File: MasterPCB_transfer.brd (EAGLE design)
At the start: 160.4 x 165.1 mm, 1072 parts, among them IC1 NCS21911SN2T1G, IC10 LDL1117S33R, IC11 LTC4222CUH#PBF, IC12 LTC4222CUH#PBF, IC13 LTC4222CUH#PBF, IC14 LTC4222CUH#PBF, IC15 LTC4222CUH#PBF, IC16 LTC4222CUH#PBF, IC17 LTC4222CUH#PBF, IC18 LTC4222CUH#PBF, IC19 LTC4222CUH#PBF, IC2 NCS21911SN2T1G, IC20 LTC4222CUH#PBF, IC21 LTC4222CUH#PBF, IC22 LTC4222CUH#PBF, IC23 LTC4222CUH#PBF, IC24 NCS21911SN2T1G, IC25 NCS21911SN2T1G, IC26 NCS21911SN2T1G, IC27 NCS21911SN2T1G, IC28 NCS21911SN2T1G, IC29 NCS21911SN2T1G, IC3 NCS21911SN2T1G, IC30 NCS21911SN2T1G, IC31 ADIS16500AMLZ, IC32 LTC6820IUD#PBF, IC33 CBTL01023GM,115, IC34 MAX889TESA+, IC35 NCS21911SN2T1G, IC36 NCS21911SN2T1G, IC37 NCS21911SN2T1G, IC38 ADS8588HIPM, IC39 NCS21911SN2T1G, IC4 LTC4222CUH#PBF, IC40 NCS21911SN2T1G, IC41 NCS21911SN2T1G, IC42 NCS21911SN2T1G, IC43 NCS21911SN2T1G, IC44 NCS21911SN2T1G, IC45 NCS21911SN2T1G, IC46 NCS21911SN2T1G, IC47 NCS21911SN2T1G, IC48 NCS21911SN2T1G, IC49 NCS21911SN2T1G, IC5 LP38692SDX-5.0_NOPB, IC50 NCS21911SN2T1G, IC51 ADS8588HIPM, IC52 ADS8588HIPM, IC53 NCS21911SN2T1G, IC54 NCS21911SN2T1G, IC55 NCS21911SN2T1G, IC56 NCS21911SN2T1G, IC57 NCS21911SN2T1G, IC58 NCS21911SN2T1G, IC59 NCS21911SN2T1G, IC6 LP38692SDX-5.0_NOPB, IC60 NCS21911SN2T1G, IC61 NCS21911SN2T1G, IC62 NCS21911SN2T1G, IC63 NCS21911SN2T1G, IC64 NCS21911SN2T1G, IC65 NCS21911SN2T1G, IC66 NCS21911SN2T1G, IC67 NCS21911SN2T1G, IC68 NCS21911SN2T1G, IC69 NCS21911SN2T1G, IC7 LDL1117S33R, IC70 NCS21911SN2T1G, IC71 NCS21911SN2T1G, IC72 NCS21911SN2T1G, IC73 NCS21911SN2T1G, IC74 NCS21911SN2T1G, IC75 NCS21911SN2T1G, IC76 NCS21911SN2T1G, IC77 NCS21911SN2T1G, IC78 NCS21911SN2T1G, IC79 NCS21911SN2T1G, IC8 LDL1117S33R, IC9 LP38692SDX-5.0_NOPB, J1 SAMTEC-SMM-104-02-X-DJ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

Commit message: Save point
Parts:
- moved C196 2.19 mm to (89.4, 42.2)
- moved C14 2.19 mm to (92.5, 26.8)
- moved C17 2.19 mm to (76.3, 31.9)
- moved C19 2.19 mm to (77.1, 29.9)
- moved C20 2.19 mm to (77.1, 36.3)
- moved C21 2.19 mm to (77.1, 38.4)
- moved C23 2.19 mm to (86.1, 42.2)
- moved C24 2.19 mm to (83.5, 42.3)
- moved C25 2.19 mm to (76.3, 34.3)
- moved IC52 2.19 mm to (86.3, 33.1)
- moved R503 1.51 mm to (130.0, 65.7)
- moved R504 1.31 mm to (132.3, 61.1)
- moved R471 0.94 mm to (130.0, 61.1)
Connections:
- removed net PG7: J12.23
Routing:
- net PF1: track 0.00 -> 77.4 mm, vias 0 -> 2
- net PG0: track 0.00 -> 77.3 mm, vias 0 -> 2
- net PG1: track 0.00 -> 71.4 mm, vias 0 -> 2
- net PG9: track 0.00 -> 71.2 mm, vias 0 -> 2
- net PG12: track 0.00 -> 71.1 mm, vias 0 -> 2
- net PG10: track 0.00 -> 68.6 mm, vias 0 -> 2
- net PG15: track 0.00 -> 62.8 mm, vias 0 -> 2
- net PG6: track 0.00 -> 57.7 mm, vias 0 -> 2
- net PG8: track 0.00 -> 56.8 mm, vias 0 -> 2
- net PG5: track 0.00 -> 54.4 mm, vias 0 -> 2
- net PG4: track 0.00 -> 52.8 mm, vias 0 -> 2
- net PG14: track 0.00 -> 52.3 mm, vias 0 -> 2
- net GND: track 0.00 -> 50.5 mm, vias 0 -> 30
- net PG3: track 0.00 -> 50.0 mm, vias 0 -> 2
- net PG2: track 0.00 -> 48.8 mm, vias 0 -> 2
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
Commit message: save point
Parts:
- moved J4 4.44 mm to (79.8, 81.9)
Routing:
- net PF11: track 0.00 -> 75.0 mm, vias 0 -> 2
- net PE6: track 0.00 -> 71.5 mm, vias 0 -> 2
- net PF2: track 0.00 -> 70.8 mm, vias 0 -> 2
- net PF9: track 0.00 -> 68.5 mm, vias 0 -> 2
- net PF8: track 0.00 -> 67.3 mm, vias 0 -> 2
- net PF3: track 0.00 -> 60.7 mm, vias 0 -> 2
- net PF6: track 0.00 -> 58.2 mm, vias 0 -> 2
- net PF7: track 0.00 -> 55.1 mm, vias 0 -> 2
- net PE5: track 0.00 -> 52.2 mm, vias 0 -> 2
- net PF10: track 0.00 -> 48.6 mm, vias 0 -> 2
- net PF4: track 0.00 -> 36.8 mm, vias 0 -> 2
- net PF5: track 0.00 -> 32.6 mm, vias 0 -> 2

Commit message: Save point
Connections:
- removed net PB13: J14.67
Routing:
- net PE0: track 0.00 -> 86.6 mm, vias 0 -> 2
- net PD15: track 0.00 -> 69.8 mm, vias 0 -> 2
- net PE1: track 0.00 -> 69.2 mm, vias 0 -> 2
- net PD14: track 0.00 -> 68.3 mm, vias 0 -> 2
- net PA3: track 0.00 -> 67.0 mm, vias 0 -> 2
- net PA12: track 0.00 -> 65.7 mm, vias 0 -> 2
- net PA5: track 0.00 -> 65.5 mm, vias 0 -> 2
- net PD11: track 0.00 -> 65.0 mm, vias 0 -> 2
- net PB7: track 0.00 -> 63.3 mm, vias 0 -> 2
- net PA6: track 0.00 -> 62.5 mm, vias 0 -> 2
- net PD12: track 0.00 -> 62.0 mm, vias 0 -> 2
- net PD13: track 0.00 -> 60.1 mm, vias 0 -> 2
- net PA11: track 0.00 -> 59.6 mm, vias 0 -> 2
- net PA10: track 0.00 -> 55.5 mm, vias 0 -> 2
- net PE3: track 0.00 -> 50.7 mm, vias 0 -> 2
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
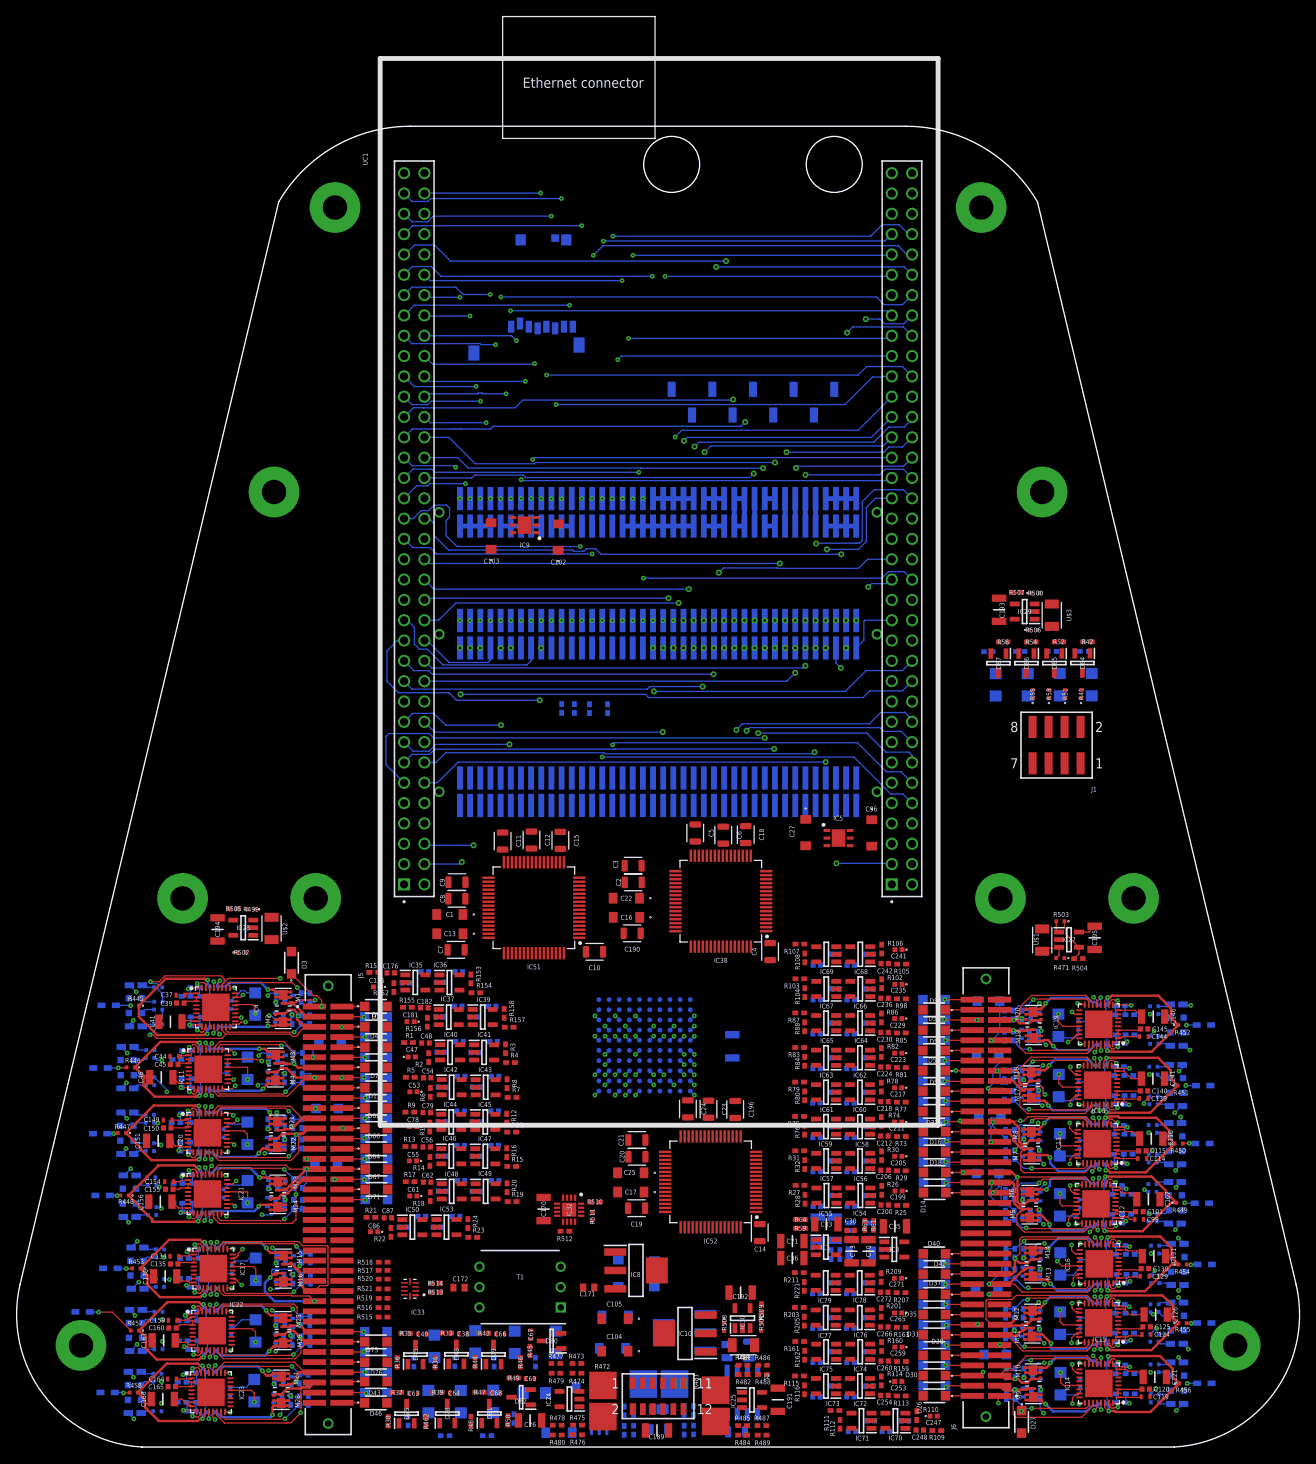
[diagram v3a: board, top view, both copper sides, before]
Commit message: New board shape
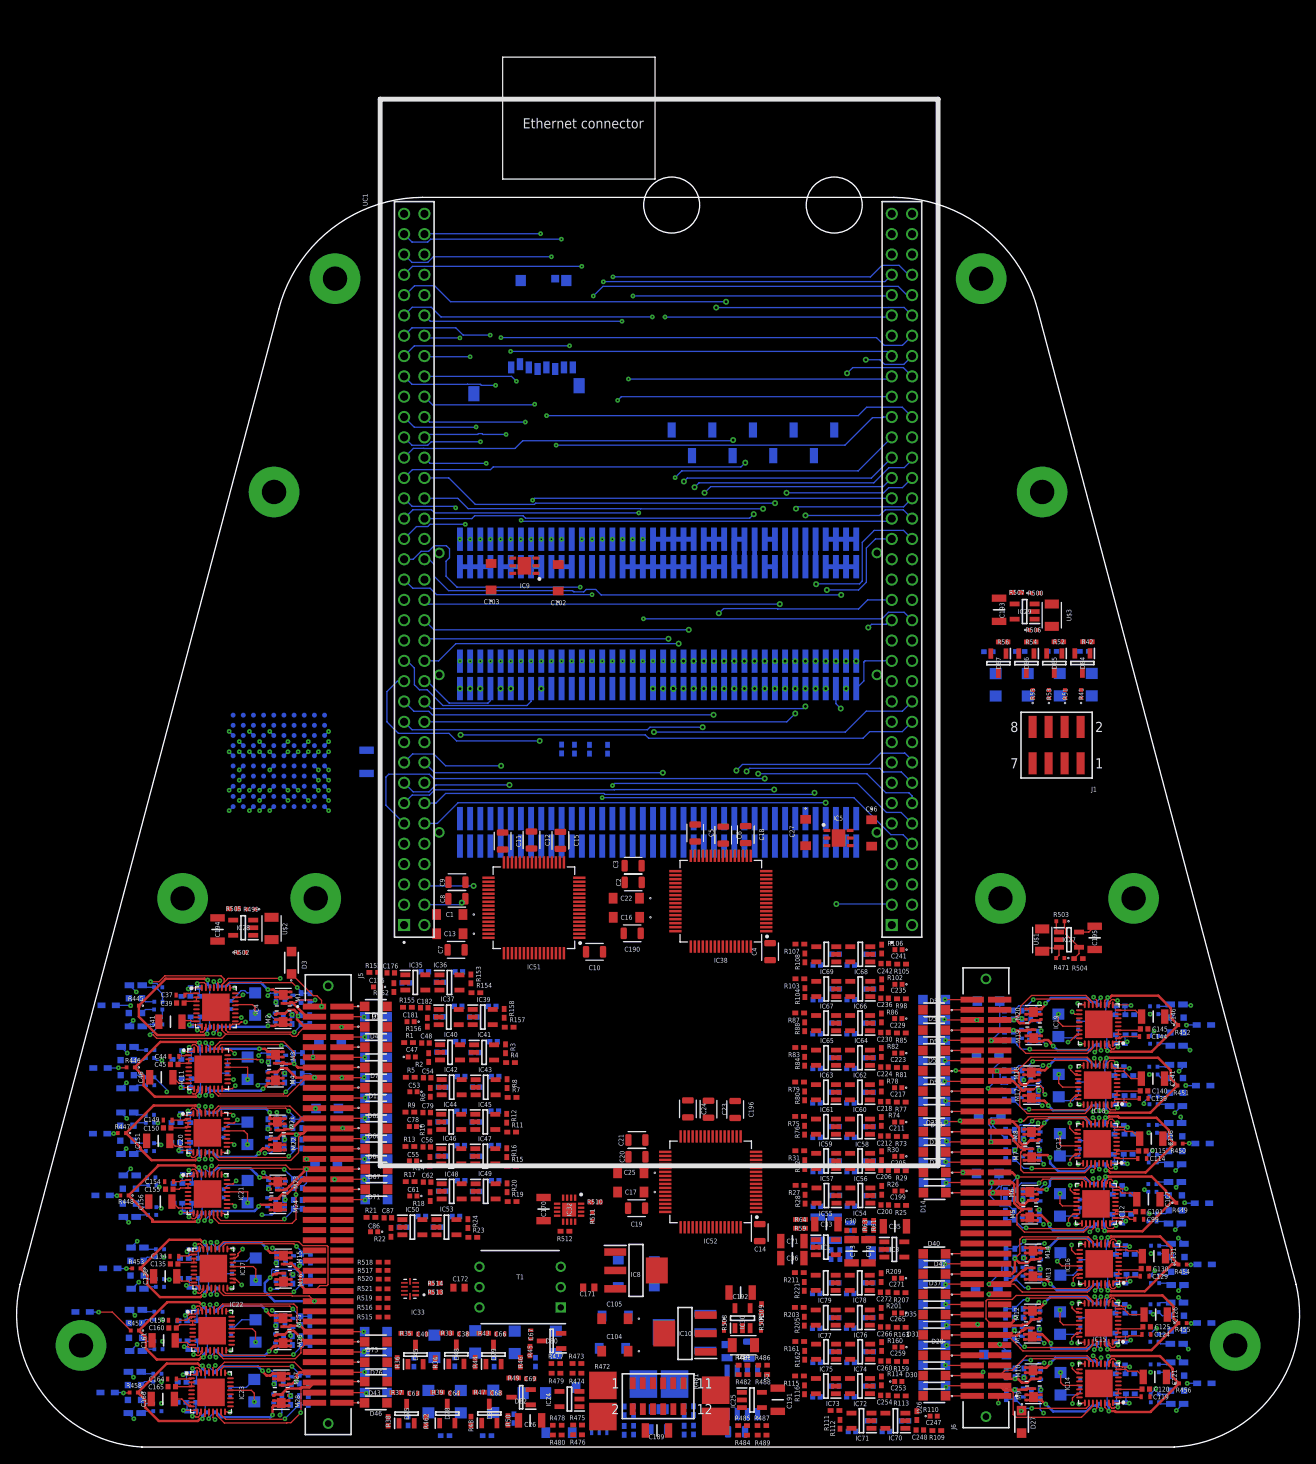
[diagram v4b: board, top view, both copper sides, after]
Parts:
- moved C169 57.9 mm to (43.3, 85.7)
- moved IC31 57.9 mm to (32.3, 85.8)
- moved U$12 8.89 mm to (120.1, 146.1)
- moved U$13 8.89 mm to (39.4, 146.1)
- moved J3 5.08 mm to (63.3, 138.6)
- moved J4 5.08 mm to (79.8, 76.8)
- moved J9 5.08 mm to (91.6, 125.5)
- moved UC1 5.08 mm to (46.4, 156.0)
- moved C102 5.08 mm to (67.3, 108.7)
- moved C103 5.08 mm to (58.9, 108.8)
- moved IC9 5.08 mm to (63.0, 110.2)
- moved J12 5.08 mm to (79.8, 111.8)
- moved J14 5.08 mm to (79.8, 96.5)
- moved R147 5.08 mm to (67.7, 87.3)
- moved R148 5.08 mm to (69.3, 87.2)
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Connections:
- net OS1_ADC: now also IC51.4
- net OS2_ADC: no longer IC51.4
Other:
- board size 160.4 x 165.1 mm -> 160.4 x 156.2 mm

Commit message: check point
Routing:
- net PC10: track 0.00 -> 76.2 mm, vias 0 -> 2
- net PC9: track 0.00 -> 75.4 mm, vias 0 -> 3
- net PC11: track 0.00 -> 73.2 mm, vias 0 -> 2
- net PC3: track 0.00 -> 68.1 mm, vias 0 -> 2
- net PC12: track 0.00 -> 65.9 mm, vias 0 -> 3
- net PC8: track 0.00 -> 64.1 mm, vias 0 -> 2
- net PC0: track 0.00 -> 57.8 mm, vias 0 -> 2
- net PC2: track 0.00 -> 56.0 mm, vias 0 -> 2
- net PC6: track 0.00 -> 53.9 mm, vias 0 -> 3
- net PC7: track 0.00 -> 32.2 mm, vias 0 -> 2
- net PD4: track 27.7 -> 27.1 mm
- net PF6: track 58.2 -> 58.7 mm

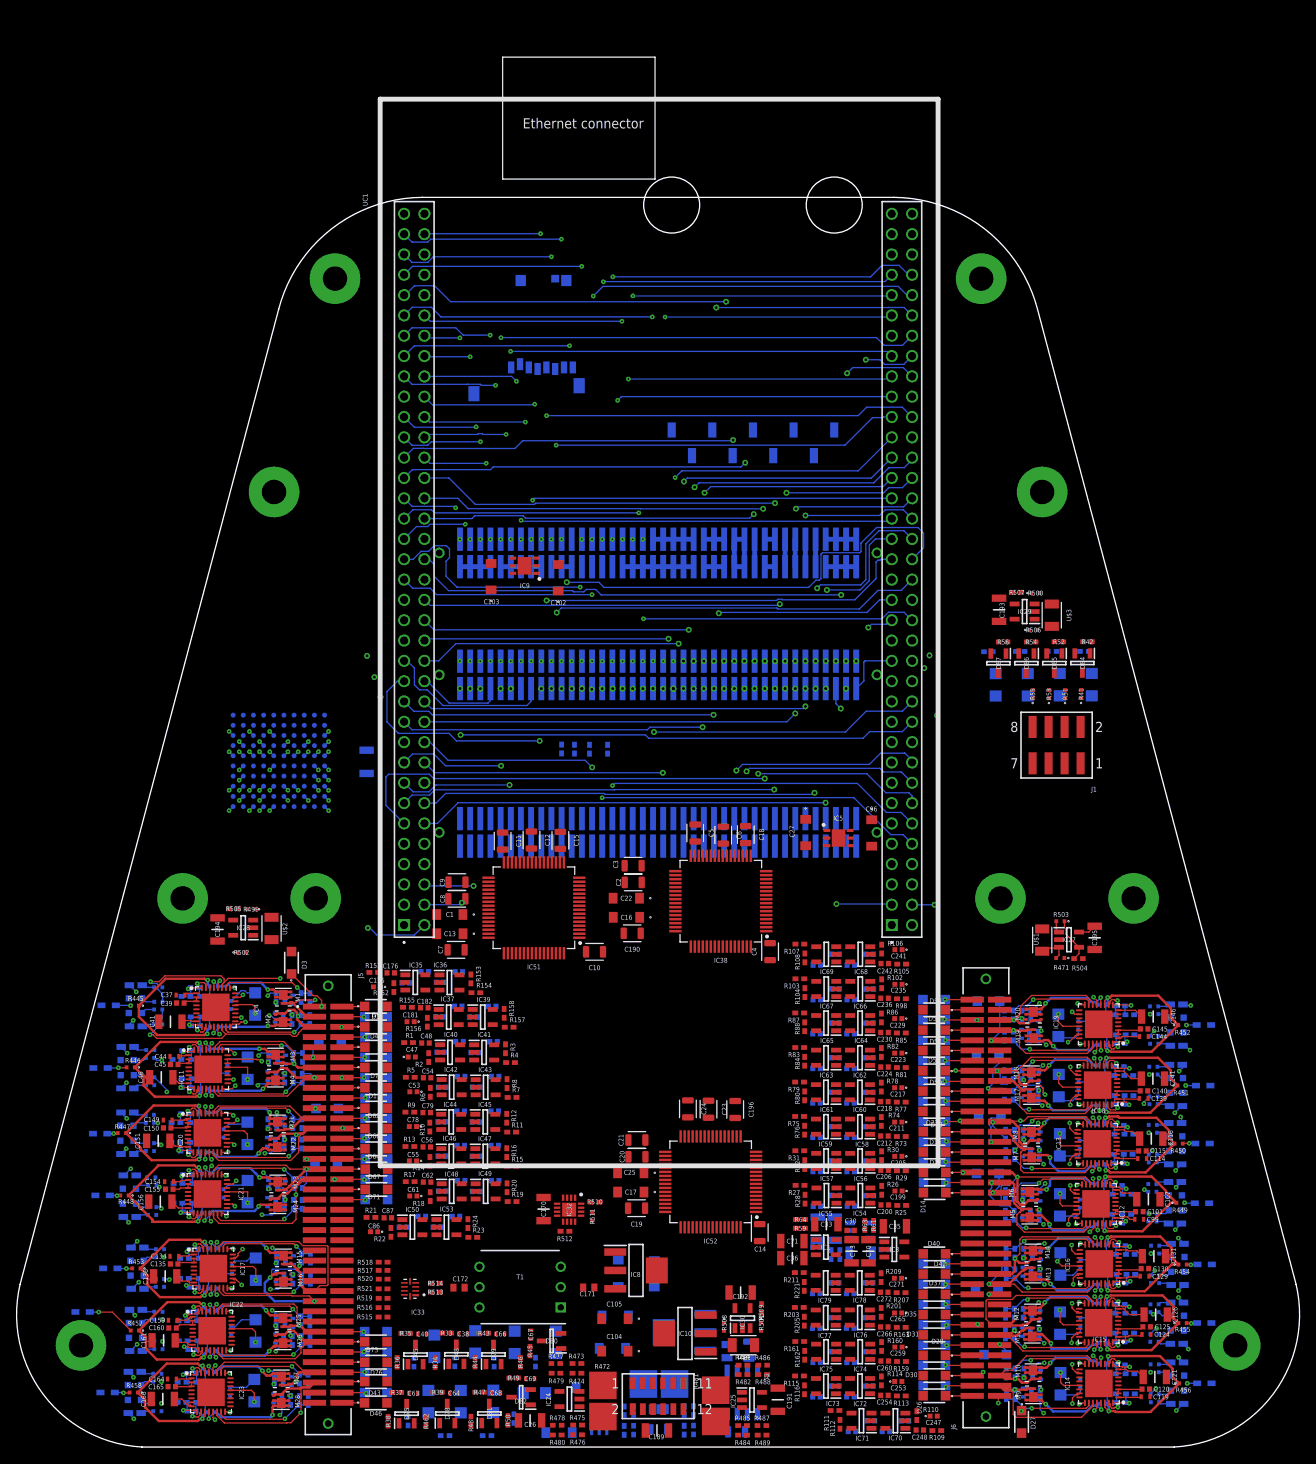
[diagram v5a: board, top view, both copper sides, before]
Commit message: New board shape
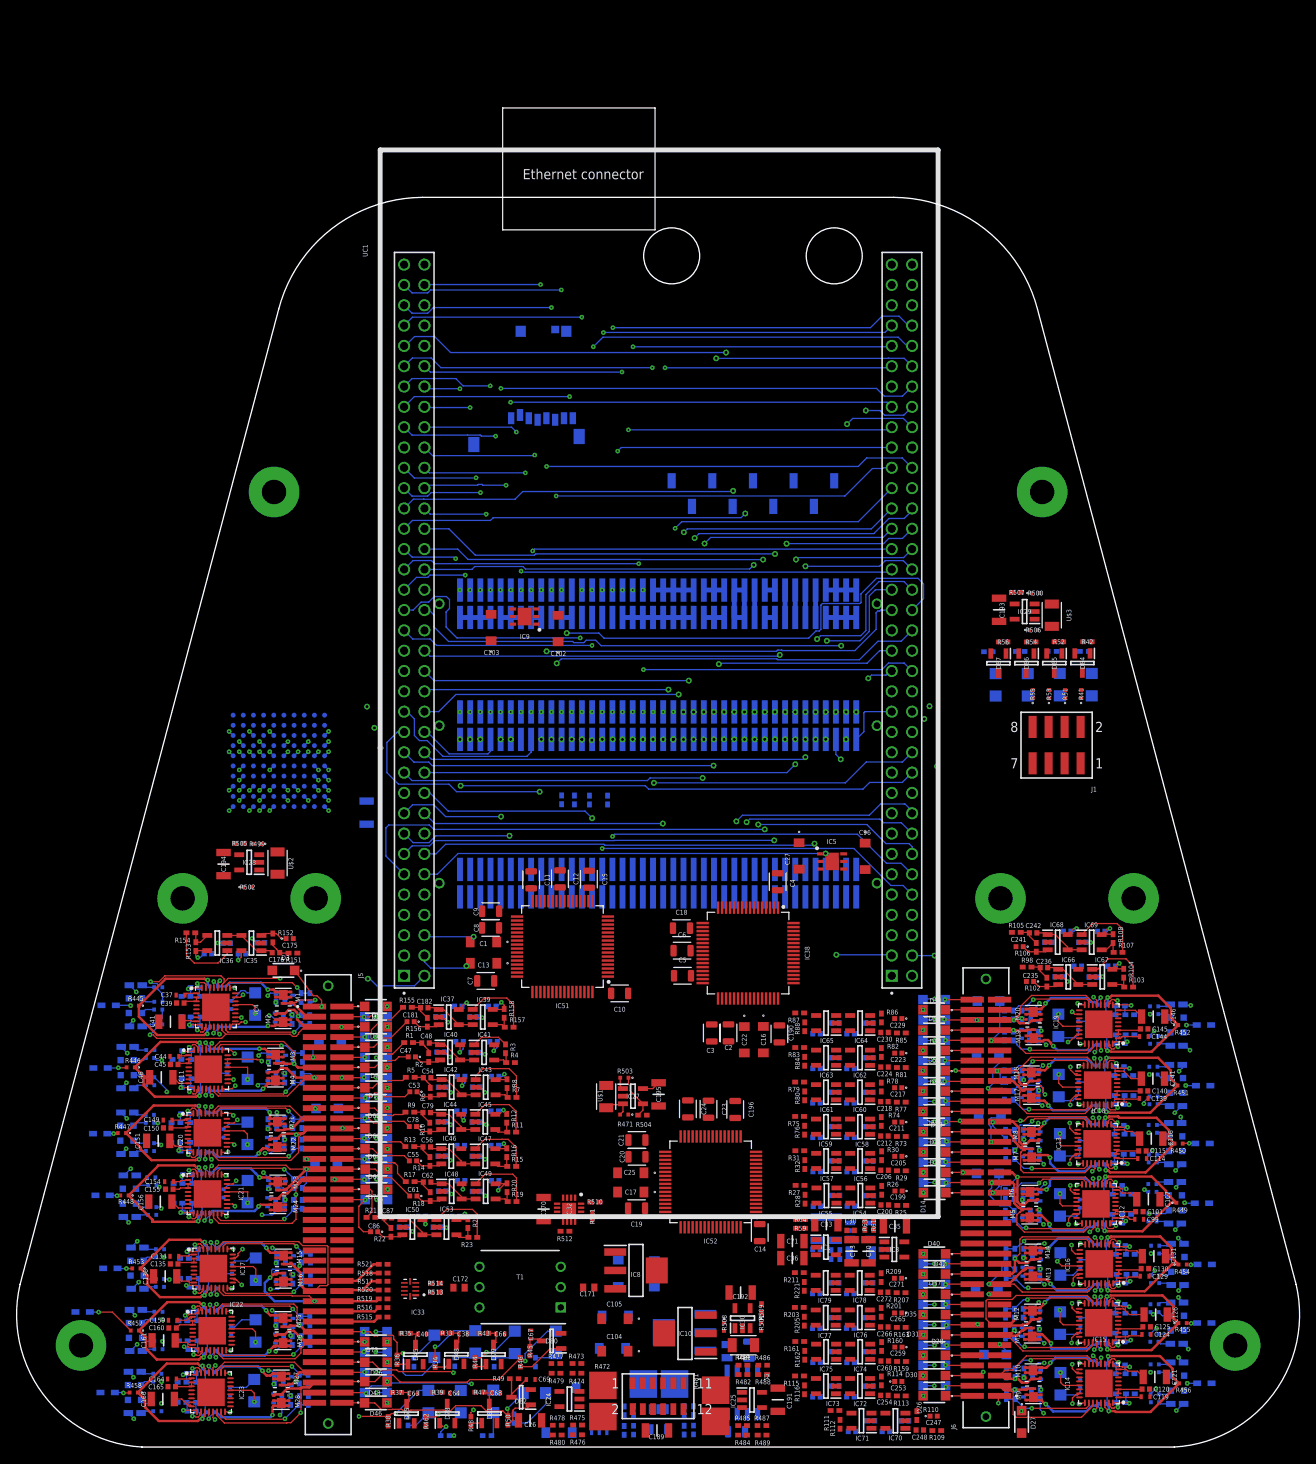
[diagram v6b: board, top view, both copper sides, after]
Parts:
- removed U$12, U$13: THROUGH_HOLE, SamacSys_Parts:1/16TH_BOLT
- moved C195 57.9 mm to (79.8, 44.1)
- moved IC27 57.9 mm to (76.6, 43.9)
- moved R471 57.9 mm to (75.5, 41.6)
- moved R503 57.9 mm to (75.5, 46.2)
- moved U$1 57.9 mm to (73.3, 43.8)
- moved R504 57.9 mm to (77.8, 41.5)
- moved R103 41.1 mm to (138.6, 57.5), turned to 180 degrees
- moved R104 39.9 mm to (138.0, 59.2), turned to 90 degrees
- moved R107 39.8 mm to (137.3, 61.8), turned to 180 degrees
- moved R108 38.6 mm to (136.6, 63.6), turned to 90 degrees
- moved C219 37.1 mm to (136.5, 60.1), turned to 0 degrees
- moved R154 36.4 mm to (21.4, 64.3), turned to 0 degrees
- moved C246 35.8 mm to (135.1, 64.4), turned to 180 degrees
- moved R153 34.6 mm to (22.0, 62.6), turned to 270 degrees
- moved IC67 34.5 mm to (135.3, 58.8), turned to 0 degrees
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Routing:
- net 5V_ON_BOARD: track 0.00 -> 48.2 mm, vias 0 -> 18
- net GND: track 50.5 -> 94.5 mm, vias 30 -> 93
- net -5V_ON_BOARD: track 0.00 -> 40.6 mm, vias 0 -> 19
- net DIN6: track 2.90 -> 31.0 mm, vias 0 -> 1
- net DIN8: track 2.83 -> 25.9 mm, vias 0 -> 1
- net DIN5: track 2.89 -> 25.5 mm, vias 1 -> 2
- net DIN4: track 2.86 -> 22.9 mm, vias 0 -> 2
- net DIN3: track 2.88 -> 21.6 mm, vias 1 -> 3
- net DIN7: track 3.29 -> 21.5 mm, vias 1 -> 3
- net DIN2: track 2.85 -> 19.6 mm, vias 0 -> 2
- net DIN1: track 2.85 -> 18.2 mm, vias 1 -> 2
- net VIN1_P: track 0.00 -> 9.19 mm
- net VIN4_P: track 0.00 -> 9.00 mm
- net VIN16_P: track 0.00 -> 8.90 mm
- net VIN2_P: track 0.00 -> 8.85 mm
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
